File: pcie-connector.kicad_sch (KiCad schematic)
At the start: 4 parts, among them J2 PCIe_x16_10146070-113Y0LF-ver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

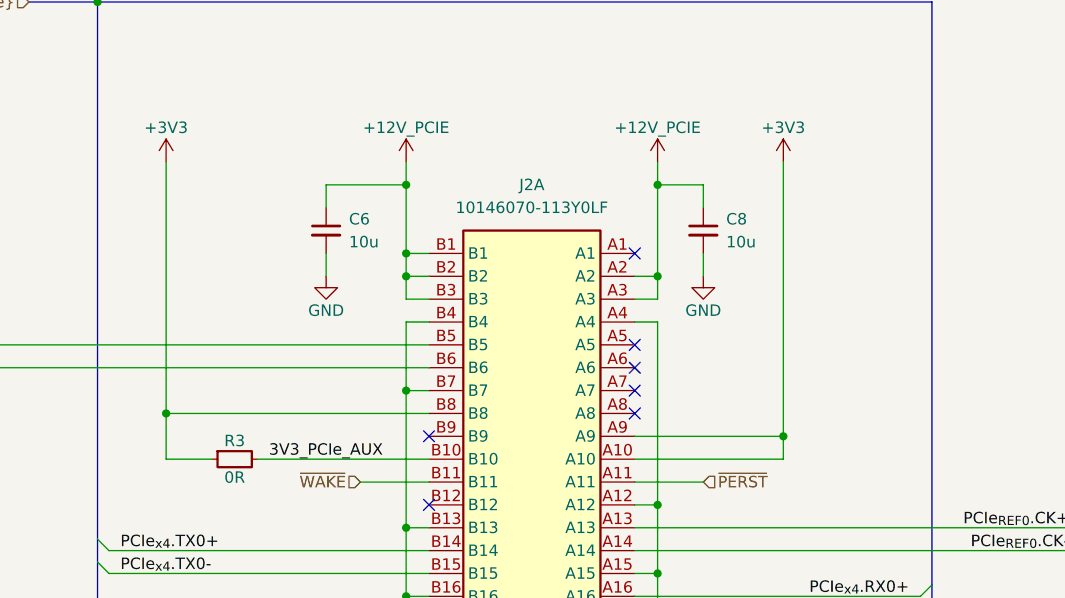
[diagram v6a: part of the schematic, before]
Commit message: [#79262] Add TVS to OCuLink connector, add decoupling capacitors for PCIe connector
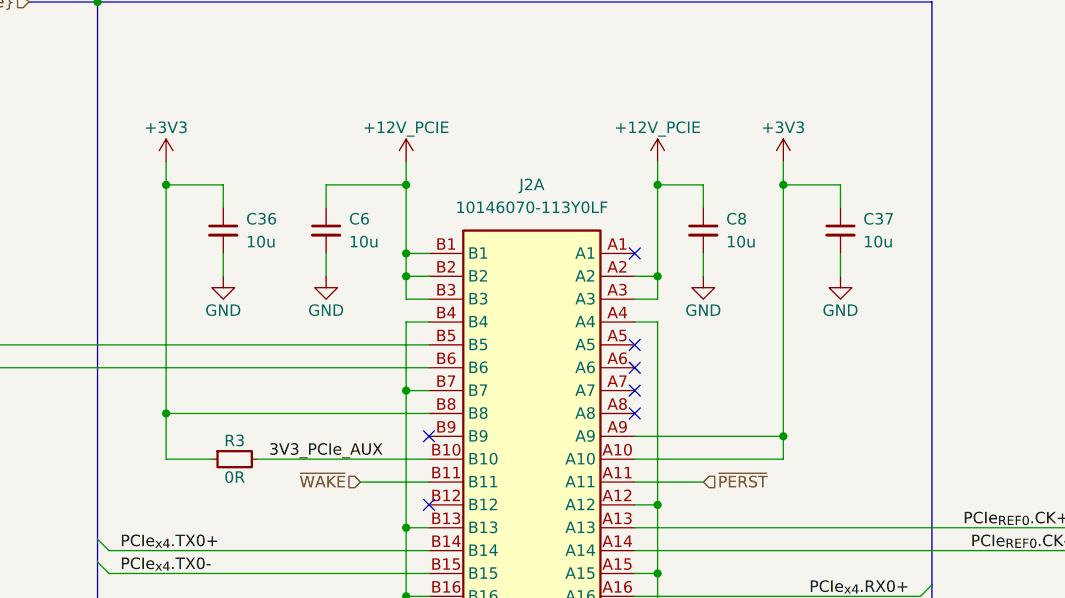
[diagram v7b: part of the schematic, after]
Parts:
- added C36, C37: C_10u_0805_35V, antmicro-footprints:C_0805_2012Metric, symbol antmicroCapacitorsmisc:C_10u_0805_35V
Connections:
- net +3V3: now also C36.1, C37.1
- net GND: now also C36.2, C37.2

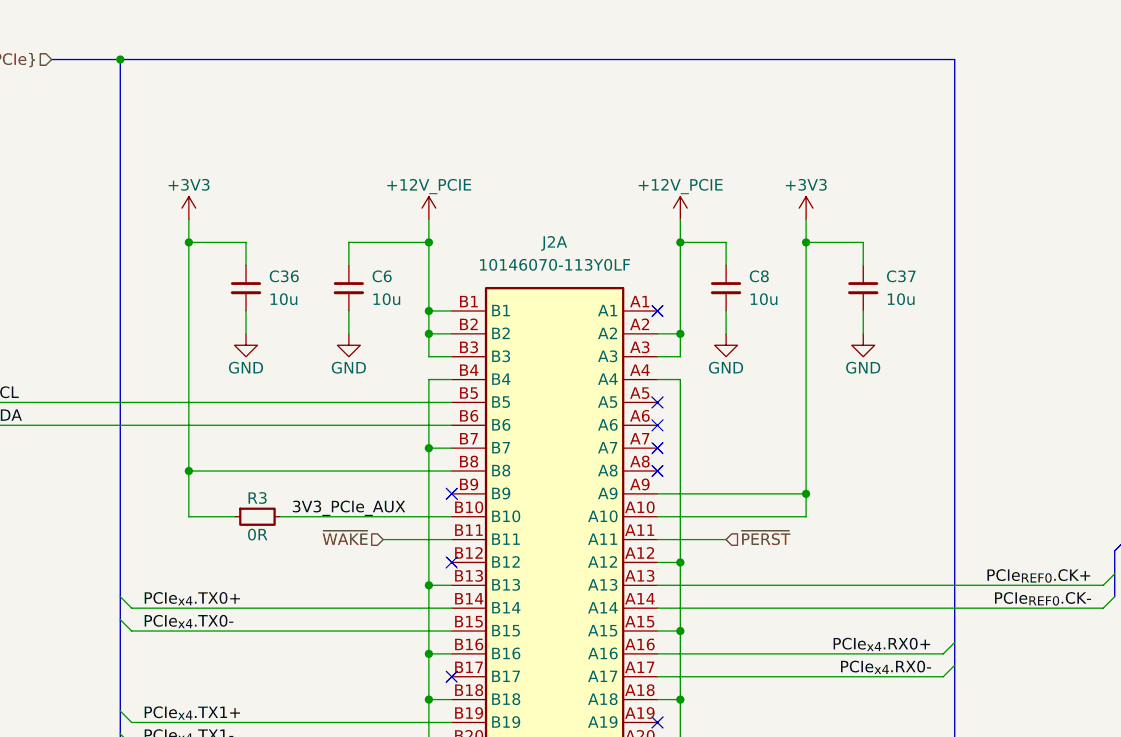
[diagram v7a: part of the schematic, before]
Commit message: [#79262] Add TVS to 12V power pins
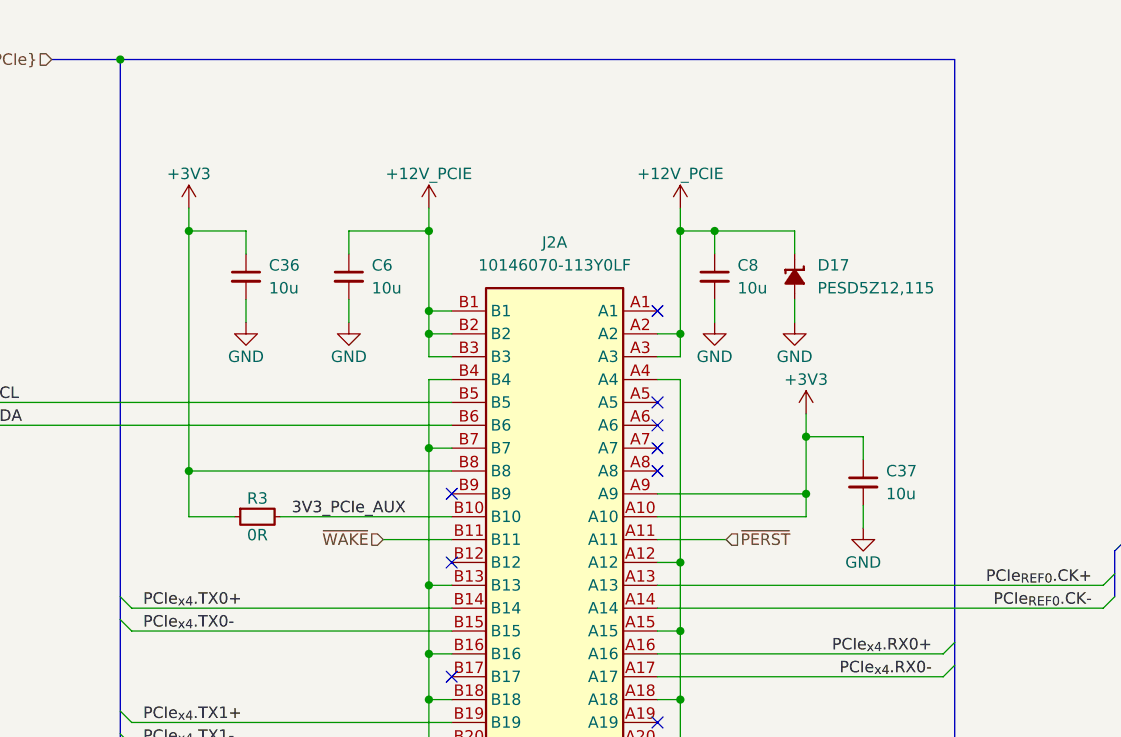
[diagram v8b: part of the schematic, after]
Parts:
- added D17: PESD5Z12, antmicro-footprints:SOD-523, symbol antmicroTVSDiodes:PESD5Z12
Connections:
- net +12V_PCIE: now also D17.1 (C)
- net GND: now also D17.2 (A)
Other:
- moved on the sheet: C36, C37, C6, C8
